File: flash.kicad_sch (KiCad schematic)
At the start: 15 parts, among them J5001 Tag-Connect_TC2050-IDC-NL_2x5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, J5002 Socket_SOP2-16_ACA-SPI-006-K0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, U5001 MT25QU01GBBB8_SOIC

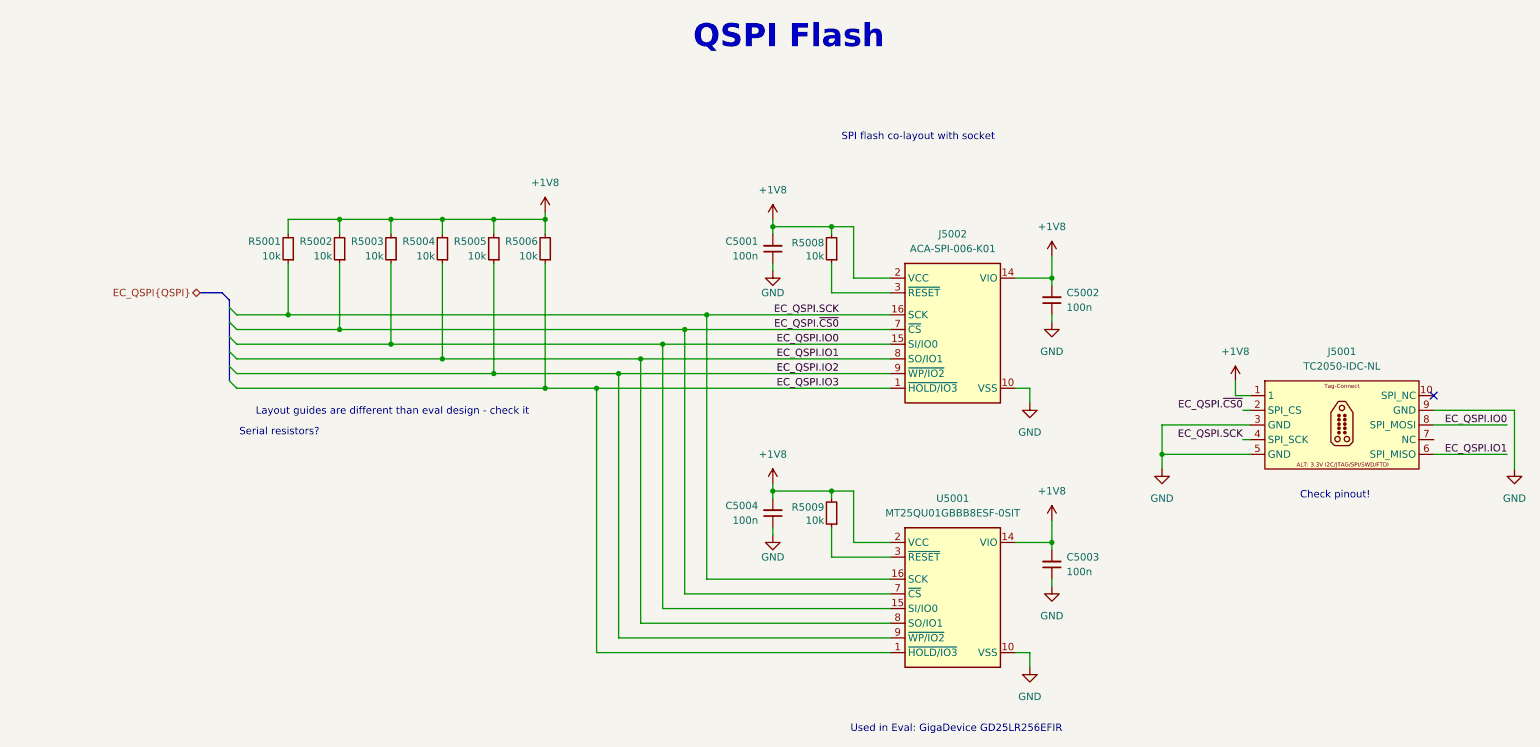
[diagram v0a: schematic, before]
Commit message: [#103224] flash: remove redundant pullup and decoupling
Duplicated but not needed due to colayout
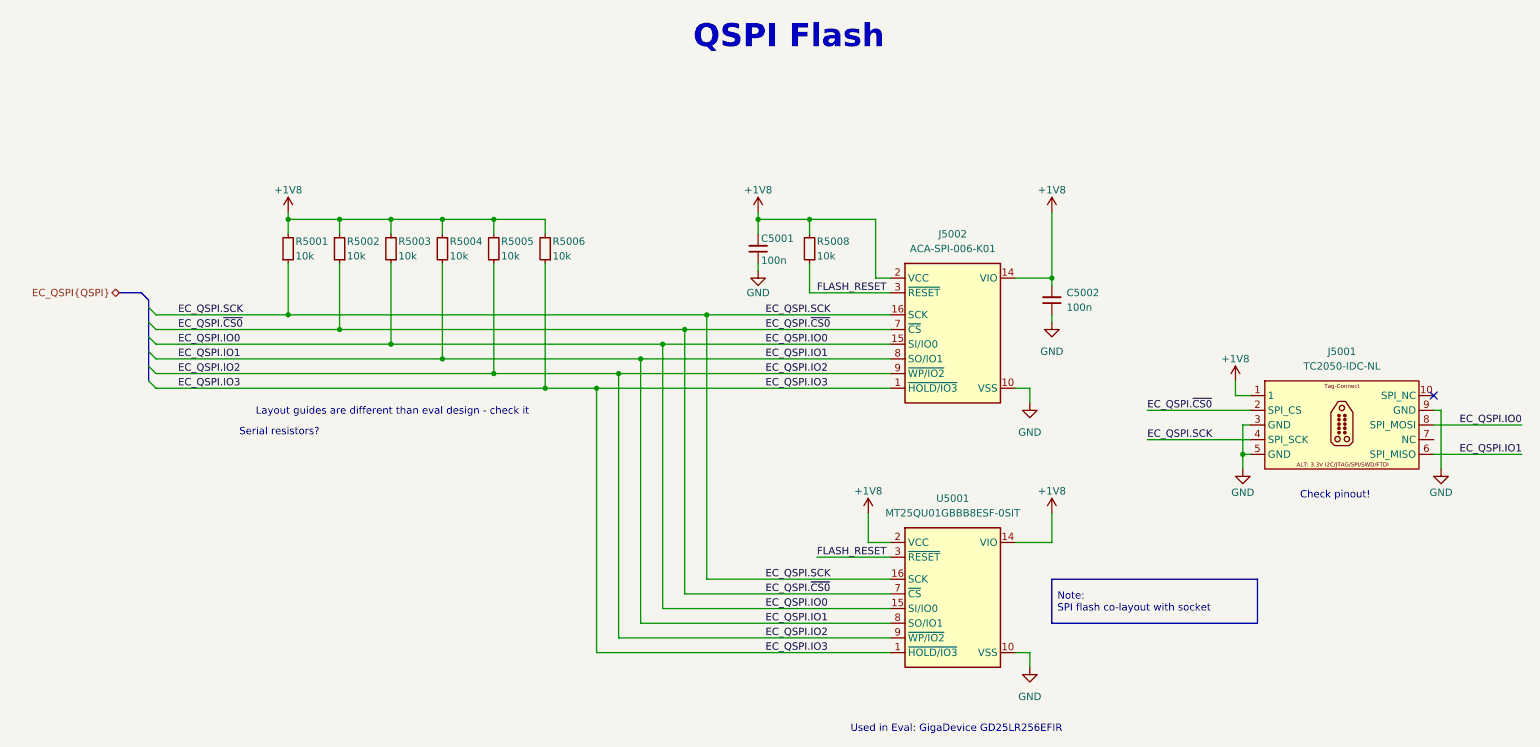
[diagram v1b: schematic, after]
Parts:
- removed C5003: C_100n_0402, antmicro-footprints:C_0402_1005Metric, symbol Capacitors0402:C_100n_0402
- removed C5004: C_100n_0402, antmicro-footprints:C_0402_1005Metric, symbol antmicroCapacitors0402:C_100n_0402
- removed R5009: R_10k_0402, antmicro-footprints:R_0402_1005Metric, symbol antmicroResistors0402:R_10k_0402
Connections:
- net FLASH_RESET: now reaches U5001.3 (~{RESET})
- net FLASH_RESET: now also J5002.3 (~{RESET}), R5008.1
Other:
- note removed: "SPI flash co-layout with socket"
- moved on the sheet: C5001, R5001, R5005, R5008

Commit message: [#103696] Add 0 ohm resistors to power rails  on the scheatic, changed C7001 from 10uF to 1uF
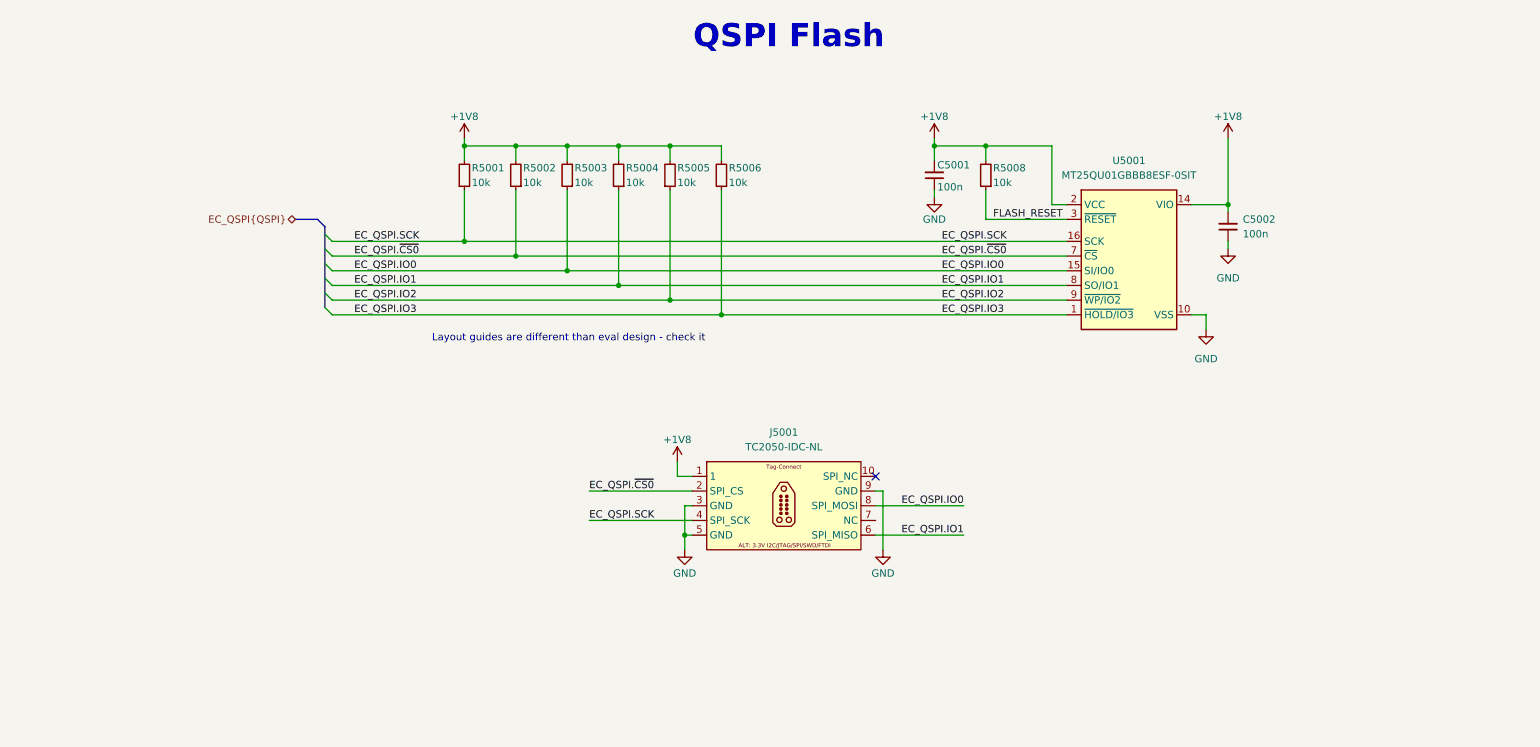
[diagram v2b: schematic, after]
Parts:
- removed J5002: Socket_SOP2-16_ACA-SPI-006-K01_Flash_CUSTOM, antmicro-footprints:Socket_SOP2-16_ACA-SPI-006-K01, symbol MechanicalParts:Socket_SOP2-16_ACA-SPI-006-K01_Flash_CUSTOM
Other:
- note removed: "Check pinout!"
- note removed: "Serial resistors?"
- note removed: "Used in Eval: GigaDevice GD25LR256EFIR"
- moved on the sheet: C5001, C5002, J5001, R5001, R5002, R5003, R5004, R5005, R5006, R5008

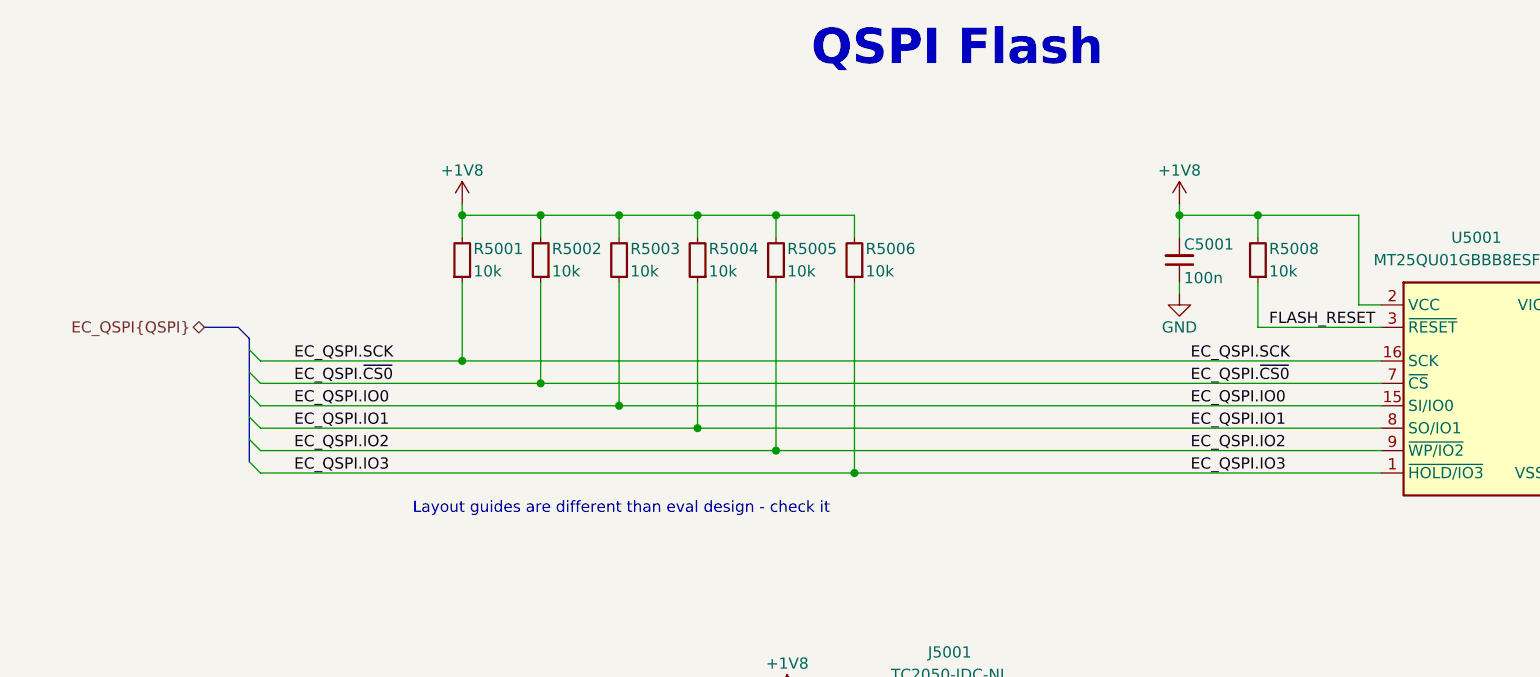
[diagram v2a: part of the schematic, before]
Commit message: [#103753] Fix issues according to the review, add FT2232 to the schematic
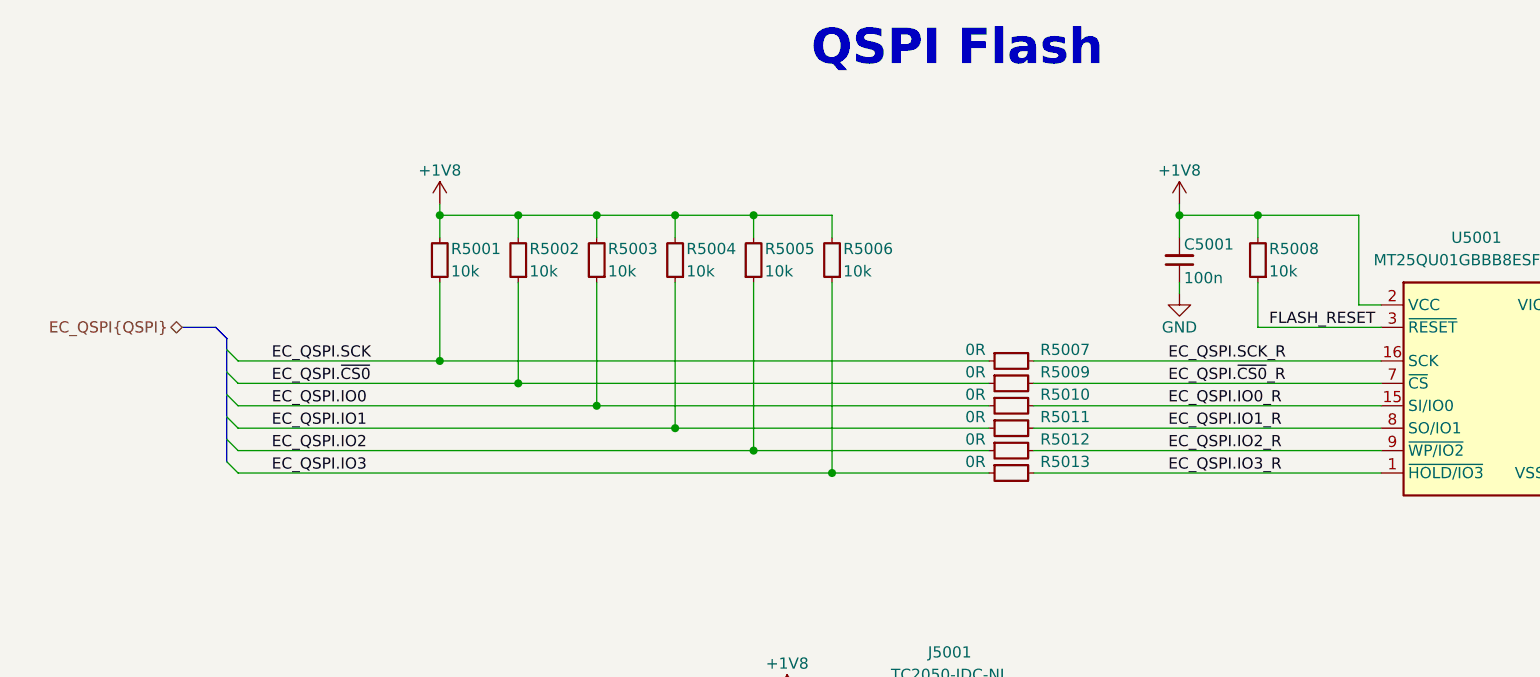
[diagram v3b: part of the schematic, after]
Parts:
- added R5007, R5009, R5010, R5011, R5012, R5013: R_0R_0402, antmicro-footprints:R_0402_1005Metric, symbol Antmicro Symbols:R_0R_0402
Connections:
- net EC_QSPI.IO0: now also R5010.1; no longer U5001.15 (SI/IO0)
- net EC_QSPI.IO1: now also R5011.1; no longer U5001.8 (SO/IO1)
- net EC_QSPI.IO2: now also R5012.1; no longer U5001.9 (~{WP/IO2})
- net EC_QSPI.IO3: now also R5013.1; no longer U5001.1 (~{HOLD/IO3})
- net EC_QSPI.SCK: now also R5007.1; no longer U5001.16 (SCK)
- net EC_QSPI.~{CS0}: now also R5009.1; no longer U5001.7 (~{CS})
- new net EC_QSPI.IO0_R: R5010.2, U5001.15 (SI/IO0)
- new net EC_QSPI.IO1_R: R5011.2, U5001.8 (SO/IO1)
- new net EC_QSPI.IO2_R: R5012.2, U5001.9 (~{WP/IO2})
- new net EC_QSPI.IO3_R: R5013.2, U5001.1 (~{HOLD/IO3})
- new net EC_QSPI.SCK_R: R5007.2, U5001.16 (SCK)
- new net EC_QSPI.~{CS0}_R: R5009.2, U5001.7 (~{CS})
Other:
- note removed: "Layout guides are different than eval design - check it"
- moved on the sheet: R5001, R5002, R5003, R5004, R5005, R5006

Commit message: [#103753] Update symbol libraries
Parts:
- C5002: symbol Capacitors0402:C_100n_0402 -> antmicroCapacitors0402:C_100n_0402
- J5001: symbol Antmicro Symbols:Tag-Connect_TC2050-IDC-NL_2x5_P1.27mm -> antmicroTestPoints:Tag-Connect_TC2050-IDC-NL_2x5_P1.27mm
- R5007, R5009, R5010, R5011, R5012, R5013: symbol Antmicro Symbols:R_0R_0402 -> antmicroResistors0402:R_0R_0402
- U5001: symbol Antmicro Symbols:MT25QU01GBBB8_SOIC -> antmicroMemory:MT25QU01GBBB8_SOIC
